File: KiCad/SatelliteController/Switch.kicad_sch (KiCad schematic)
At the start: 41 parts, among them U5 U74HC14

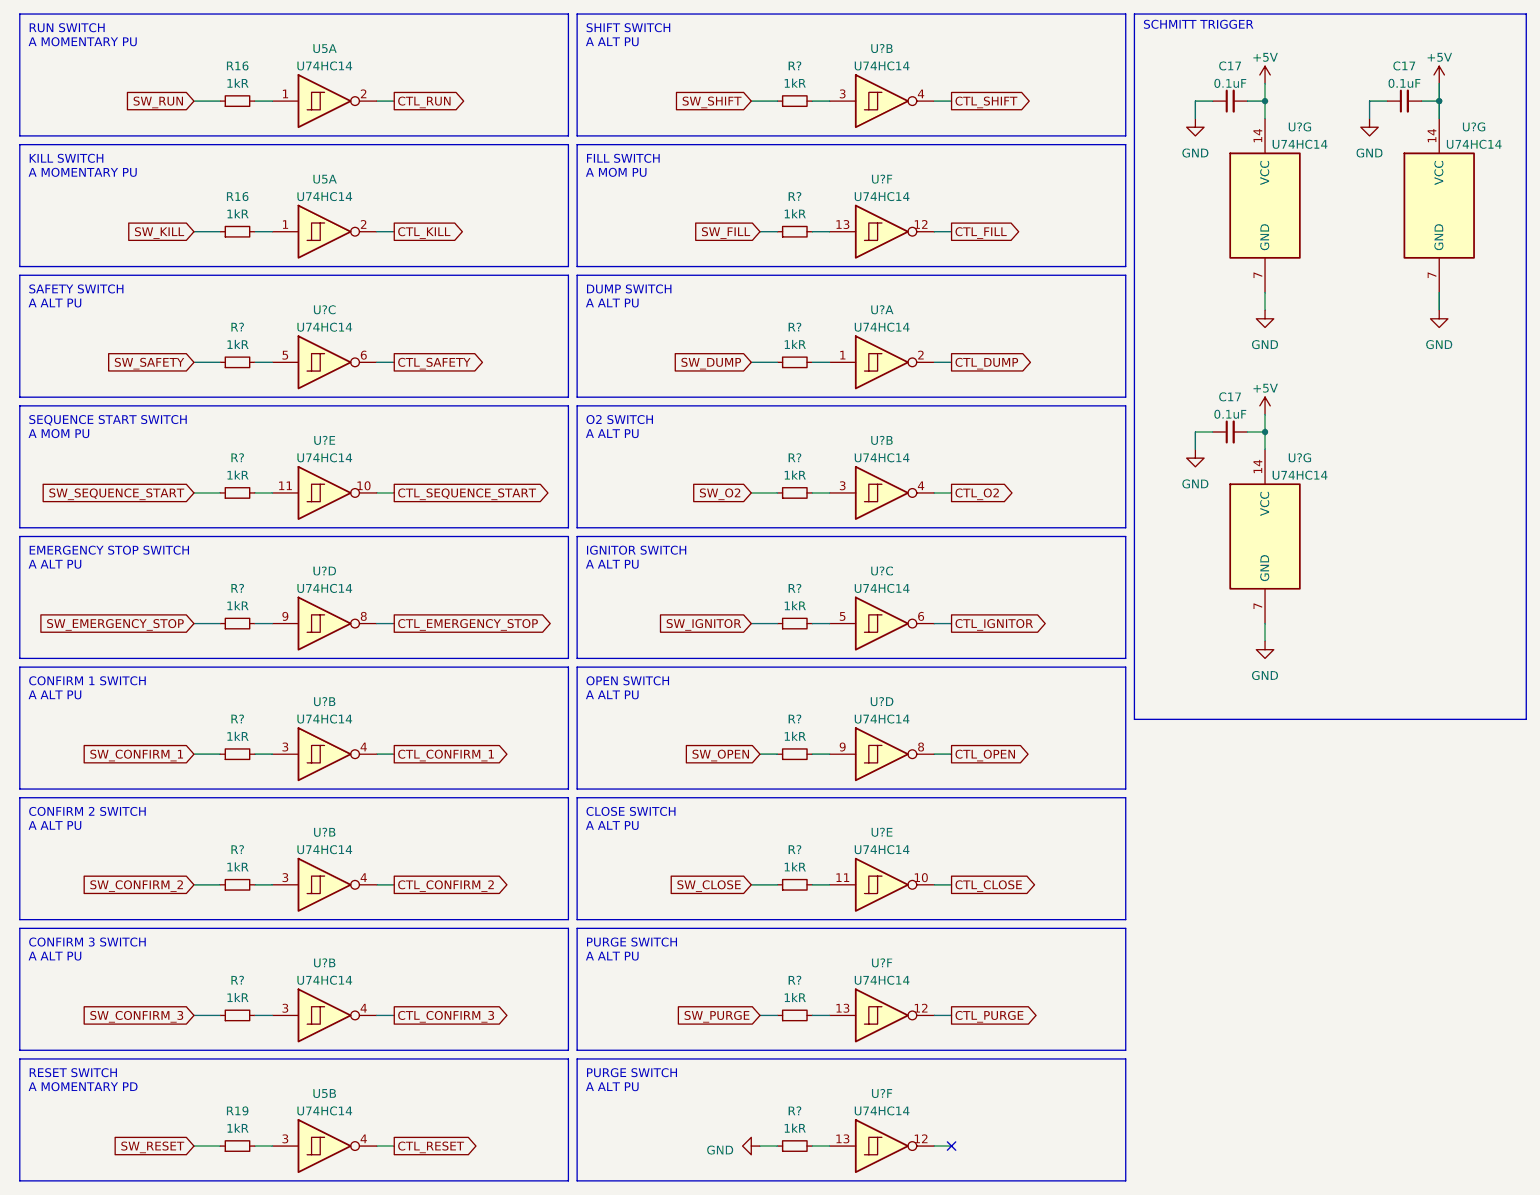
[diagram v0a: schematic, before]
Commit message: 圧力センサとの接続部を追加
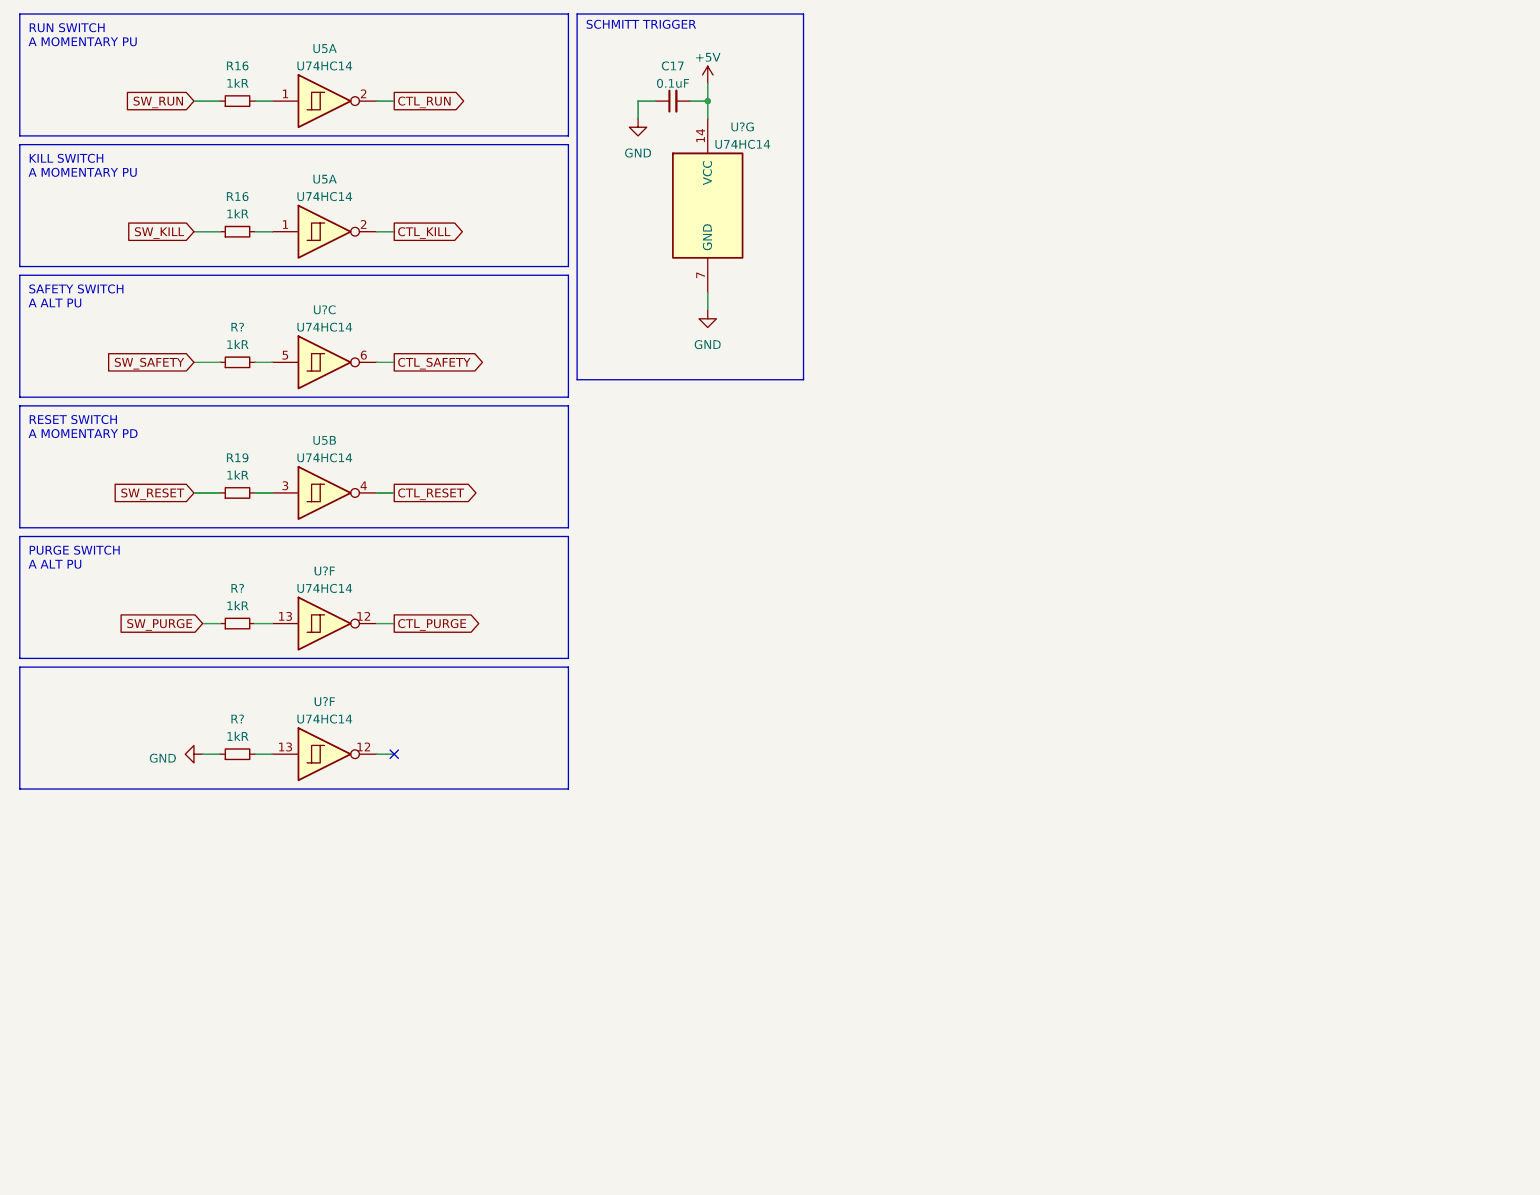
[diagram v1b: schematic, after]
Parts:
- removed C17 (x2): 0.1uF, Capacitor_SMD:C_0603_1608Metric_Pad1.08x0.95mm_HandSolder, symbol Device:C_Small
- removed R? (x12): 1kR, Resistor_SMD:R_0603_1608Metric_Pad0.98x0.95mm_HandSolder, symbol Device:R_Small
- removed U? (x14): U74HC14, Package_SO:TSSOP-14_4.4x5mm_P0.65mm, symbol 74xx:74HC14
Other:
- note removed: "CLOSE SWITCH A ALT PU"
- note removed: "CONFIRM 1 SWITCH A ALT PU"
- note removed: "CONFIRM 2 SWITCH A ALT PU"
- note removed: "CONFIRM 3 SWITCH A ALT PU"
- note removed: "DUMP SWITCH A ALT PU"
- note removed: "EMERGENCY STOP SWITCH A ALT PU"
- note removed: "FILL SWITCH A MOM PU"
- note removed: "IGNITOR SWITCH A ALT PU"
- note removed: "O2 SWITCH A ALT PU"
- note removed: "OPEN SWITCH A ALT PU"
- note removed: "SEQUENCE START SWITCH A MOM PU"
- note removed: "SHIFT SWITCH A ALT PU"
- moved on the sheet: C17, R19, R?, U5B, U?F, U?G

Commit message: ランコンのKiCadプロジェクトをコピーしてサテコンを作成
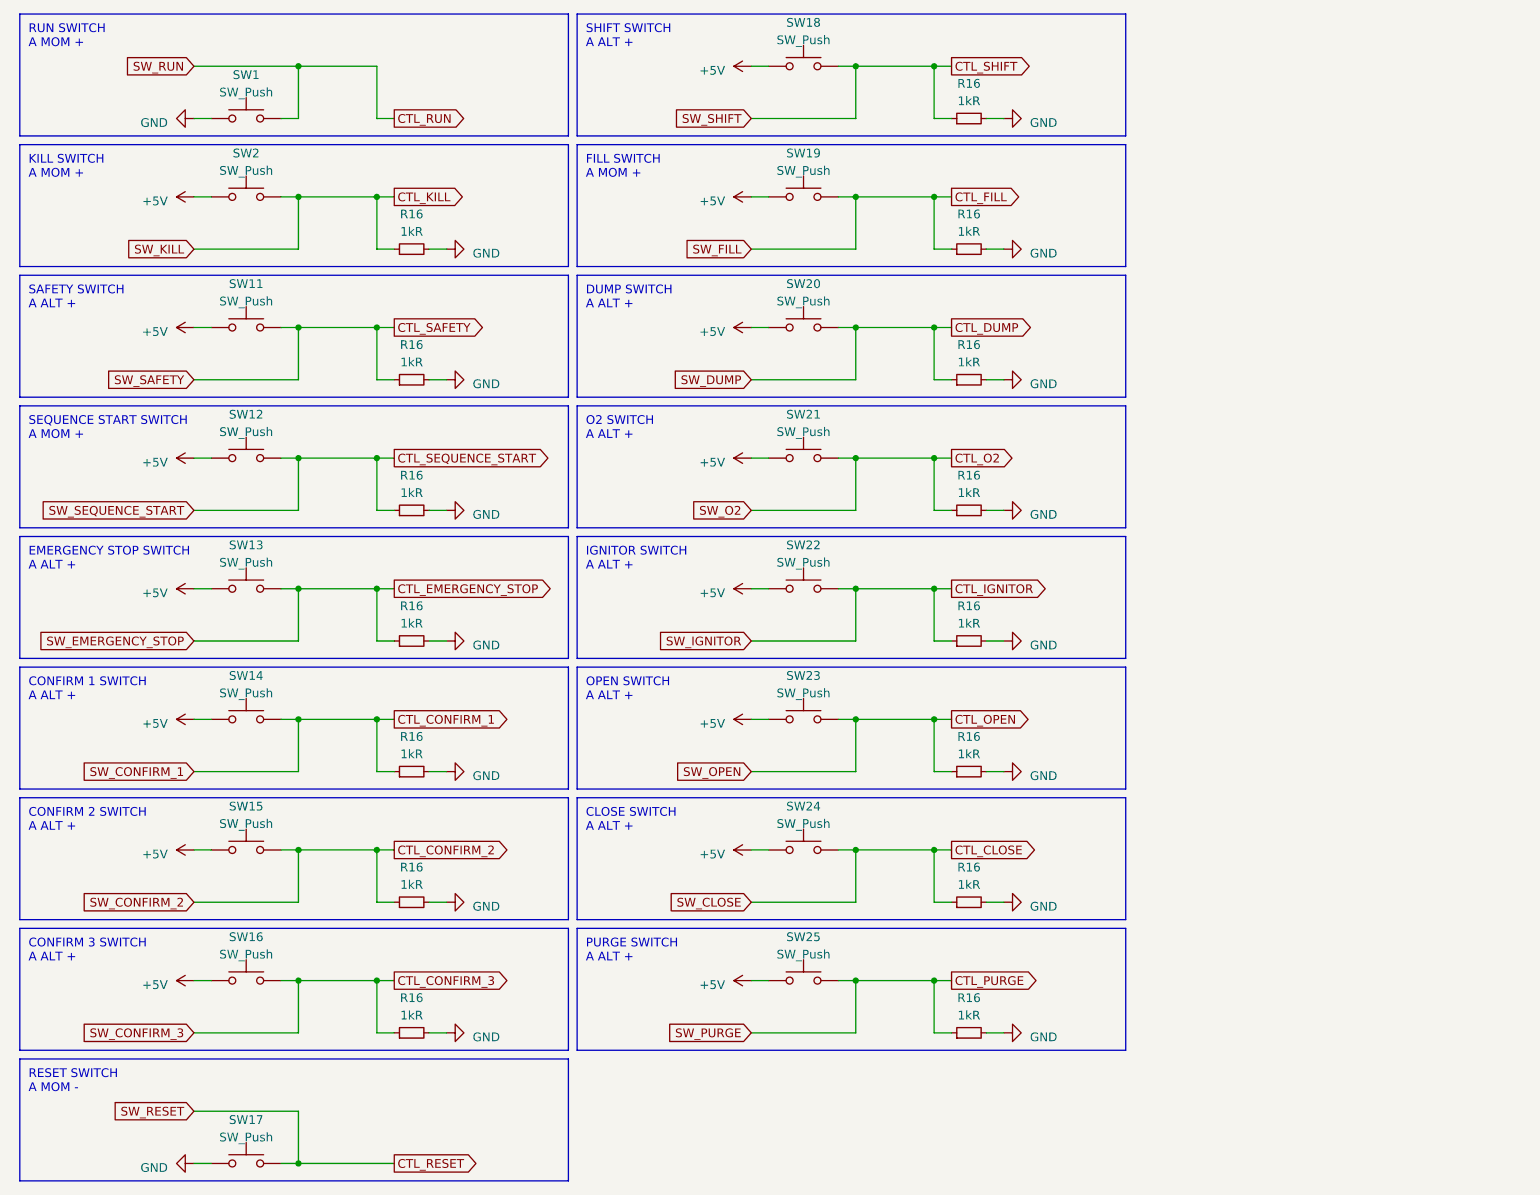
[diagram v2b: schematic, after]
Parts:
- removed C17: 0.1uF, Capacitor_SMD:C_0603_1608Metric_Pad1.08x0.95mm_HandSolder, symbol Device:C_Small
- removed R16 (x2), R19, R? (x3): 1kR, Resistor_SMD:R_0603_1608Metric_Pad0.98x0.95mm_HandSolder, symbol Device:R_Small
- removed U5, U? (x4): U74HC14, Package_SO:TSSOP-14_4.4x5mm_P0.65mm, symbol 74xx:74HC14
- added R16 (x15): 1kR, Resistor_SMD:R_0603_1608Metric_Pad0.98x0.95mm_HandSolder, symbol Device:R_Small
- added SW1, SW17, SW2: SW_Push, TSRP_Button_Switch_SMD:TVAF06-A020B-R, symbol Switch:SW_Push
- added SW11, SW12, SW13, SW14, SW15, SW16, SW18, SW19, SW20, SW21, SW22, SW23, SW24, SW25: SW_Push, Connector_PinHeader_2.54mm:PinHeader_1x02_P2.54mm_Vertical, symbol Switch:SW_Push
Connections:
- net +5V: now also SW11.1, SW12.1, SW13.1, SW14.1, SW15.1, SW16.1, SW18.1, SW19.1, SW2.1, SW20.1, SW21.1, SW22.1, SW23.1, SW24.1, SW25.1
- net CTL_KILL: now also R16.1, SW2.2
- net CTL_PURGE: now also R16.1, SW25.2
- net CTL_RESET: now also SW17.2
- net CTL_RUN: now also SW1.2
- net CTL_SAFETY: now also R16.1, SW11.2
- net GND: now also R16.2, R16.2, R16.2, R16.2, R16.2, R16.2, R16.2, R16.2, R16.2, R16.2, R16.2, R16.2, R16.2, R16.2, R16.2, SW1.1, SW17.1
- new net CTL_CLOSE: R16.1, SW24.2
- new net CTL_CONFIRM_1: R16.1, SW14.2
- new net CTL_CONFIRM_2: R16.1, SW15.2
- new net CTL_CONFIRM_3: R16.1, SW16.2
- new net CTL_DUMP: R16.1, SW20.2
- new net CTL_EMERGENCY_STOP: R16.1, SW13.2
- new net CTL_FILL: R16.1, SW19.2
- new net CTL_IGNITOR: R16.1, SW22.2
- new net CTL_O2: R16.1, SW21.2
- new net CTL_OPEN: R16.1, SW23.2
- new net CTL_SEQUENCE_START: R16.1, SW12.2
- new net CTL_SHIFT: R16.1, SW18.2
- no-connect marks 1 -> 0
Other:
- note added: "CLOSE SWITCH A ALT +"
- note added: "CONFIRM 1 SWITCH A ALT +"
- note added: "CONFIRM 2 SWITCH A ALT +"
- note added: "CONFIRM 3 SWITCH A ALT +"
- note added: "DUMP SWITCH A ALT +"
- note added: "EMERGENCY STOP SWITCH A ALT +"
- note added: "FILL SWITCH A MOM +"
- note added: "IGNITOR SWITCH A ALT +"
- note added: "KILL SWITCH A MOM +"
- note added: "O2 SWITCH A ALT +"
- note added: "OPEN SWITCH A ALT +"
- note added: "PURGE SWITCH A ALT +"
- note added: "RESET SWITCH A MOM -"
- note added: "RUN SWITCH A MOM +"
- note added: "SAFETY SWITCH A ALT +"
- note added: "SEQUENCE START SWITCH A MOM +"
- note added: "SHIFT SWITCH A ALT +"
- note removed: "KILL SWITCH A MOMENTARY PU"
- note removed: "PURGE SWITCH A ALT PU"
- note removed: "RESET SWITCH A MOMENTARY PD"
- note removed: "RUN SWITCH A MOMENTARY PU"
- note removed: "SAFETY SWITCH A ALT PU"
- note removed: "SCHMITT TRIGGER"

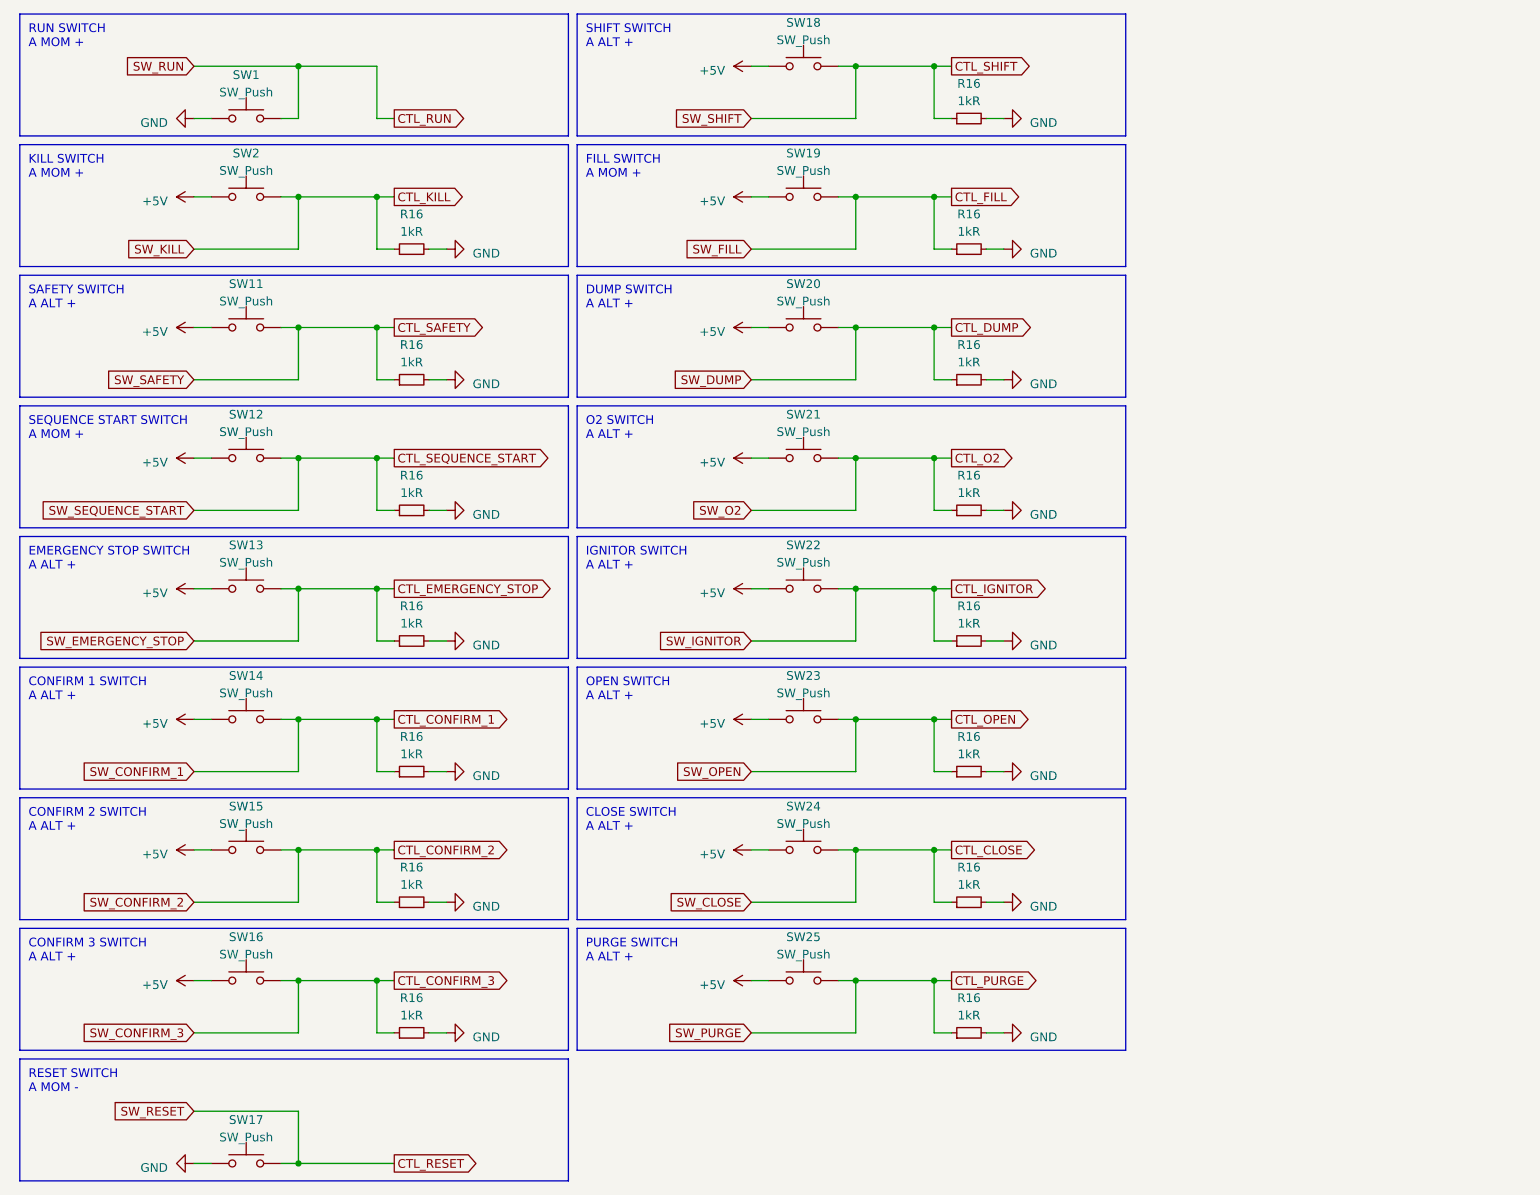
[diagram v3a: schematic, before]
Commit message: 手動操作を削除
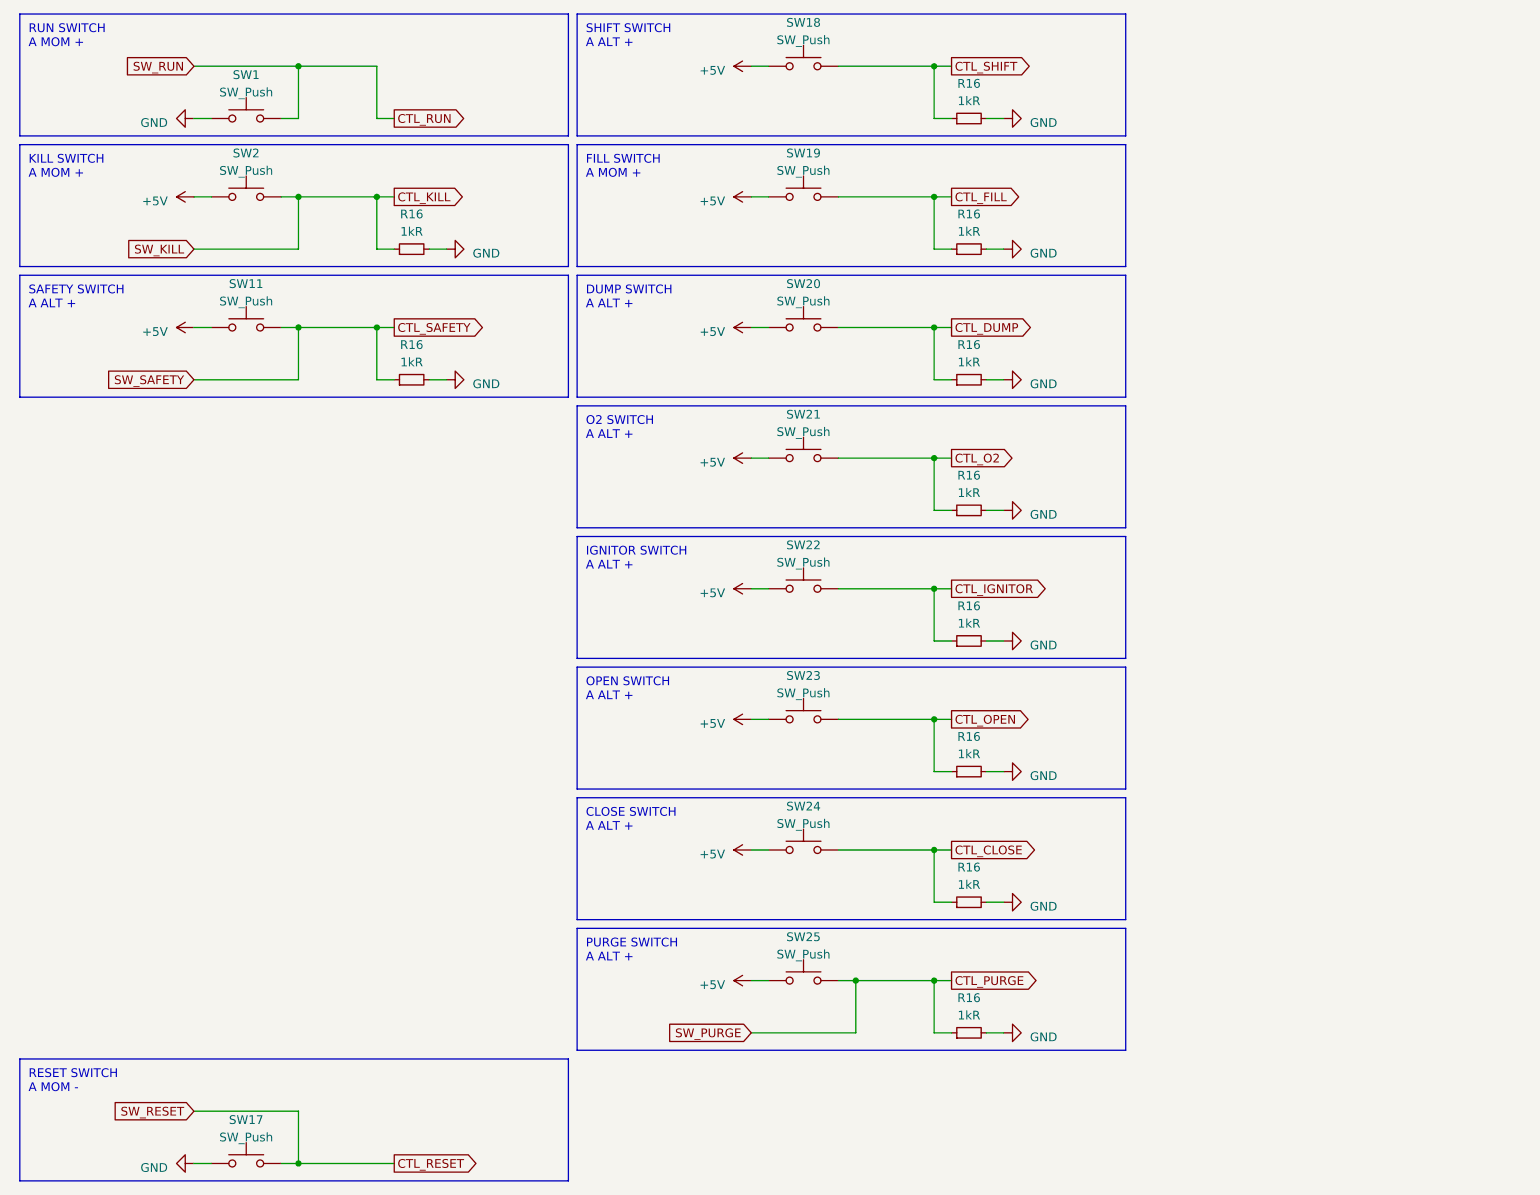
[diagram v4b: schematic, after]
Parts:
- removed R16 (x5): 1kR, Resistor_SMD:R_0603_1608Metric_Pad0.98x0.95mm_HandSolder, symbol Device:R_Small
- removed SW12, SW13, SW14, SW15, SW16: SW_Push, Connector_PinHeader_2.54mm:PinHeader_1x02_P2.54mm_Vertical, symbol Switch:SW_Push
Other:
- note removed: "CONFIRM 1 SWITCH A ALT +"
- note removed: "CONFIRM 2 SWITCH A ALT +"
- note removed: "CONFIRM 3 SWITCH A ALT +"
- note removed: "EMERGENCY STOP SWITCH A ALT +"
- note removed: "SEQUENCE START SWITCH A MOM +"
